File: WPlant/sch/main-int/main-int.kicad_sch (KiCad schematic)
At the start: 70 parts, among them J1 PROG/JTAG, J10 Ext, J8 eInk-Buttons, J9 Leak, M1 Motor_DC, Q6 Si2301, Q7 BC817, SW1 SW_Push, SW2 SW_Push, SW3 SW_Push, U1 SIWG917Y121MGABAR, U10 SP485EEN-L/TR, U11 TXU0102QDCURQ1, U5 TC4427AEOA713, U8 NC7S02P5, U9 INA180A2, X1 SIT1552AI-JE-DCC-32.768D

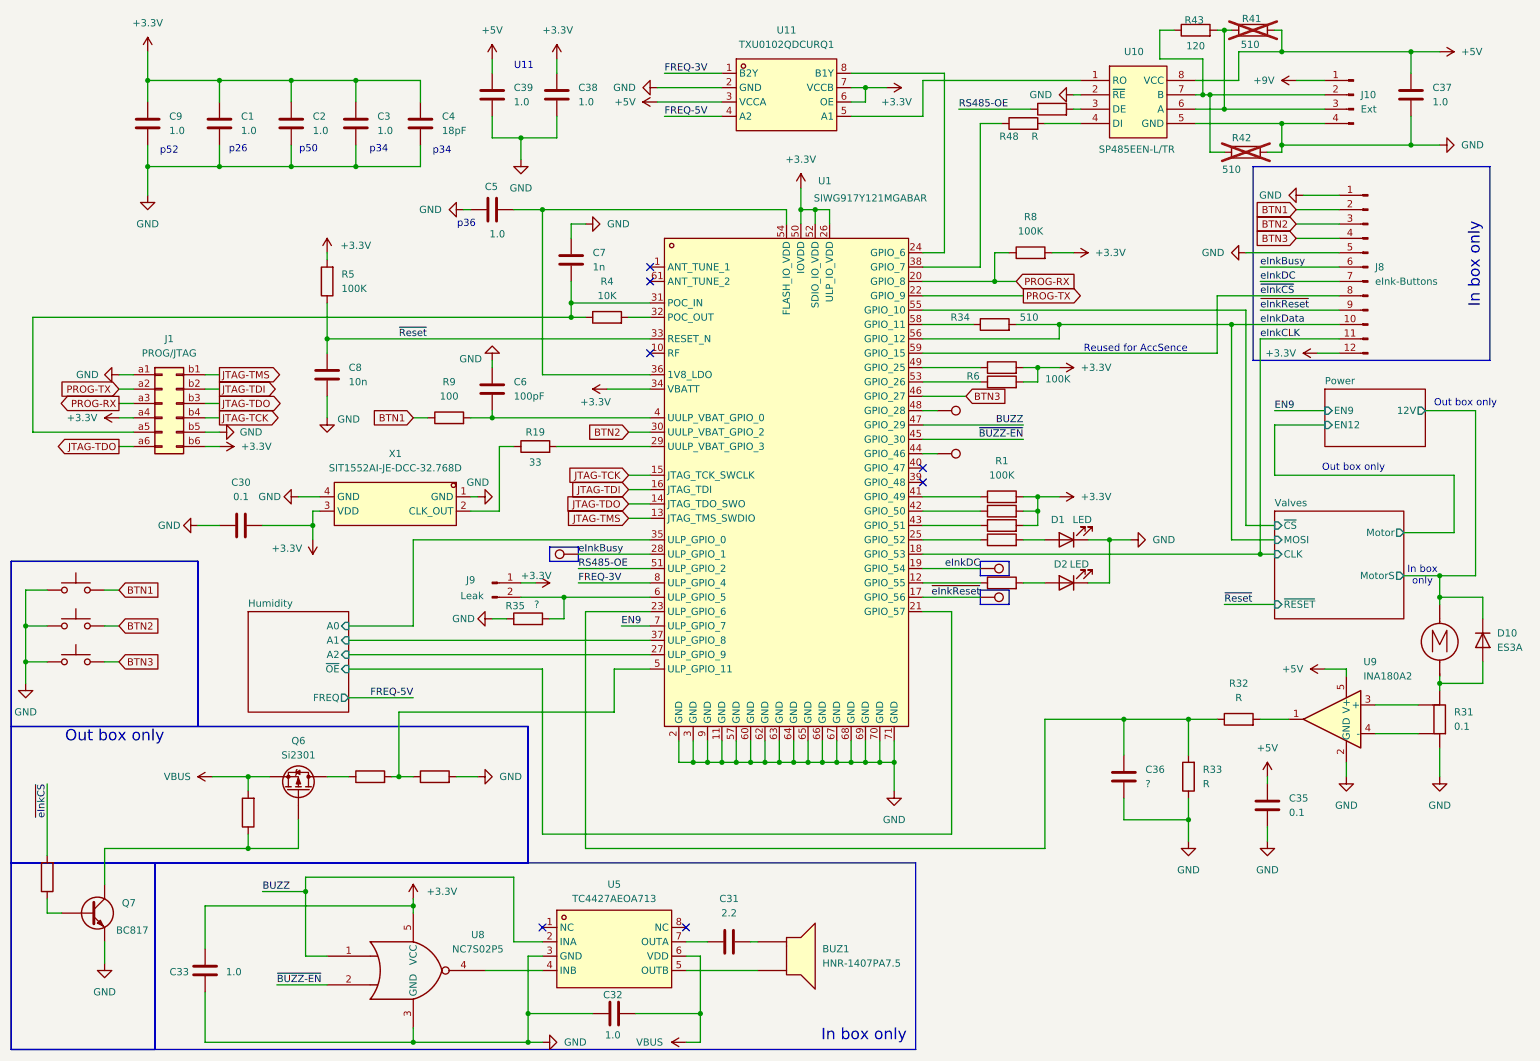
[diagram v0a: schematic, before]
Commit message: Generic design was splited to Main-Int and Main-Ext
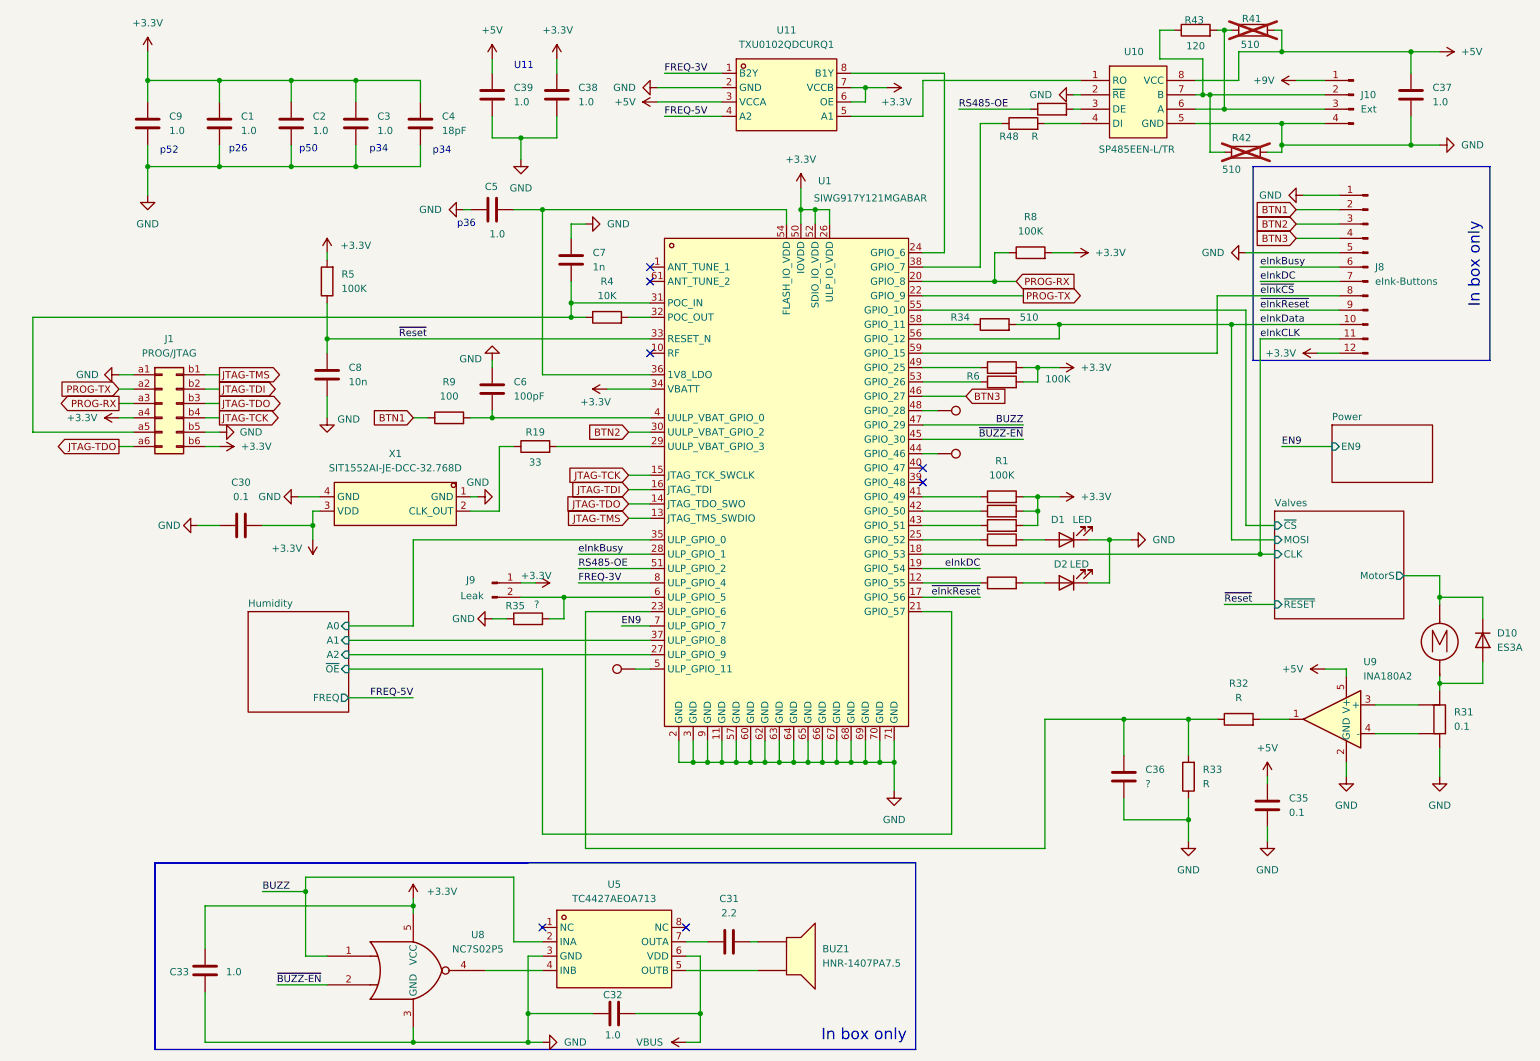
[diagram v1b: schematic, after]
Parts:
- removed Q6: Si2301, Package_TO_SOT_SMD:SOT-23, symbol Device:Q_PMOS_GSD
- removed Q7: BC817, Package_TO_SOT_SMD:SOT-23, symbol Transistor_BJT:BC817
- removed R36, R37, R38, R39: 100K, Resistor_SMD:R_0603_1608Metric_Pad0.98x0.95mm_HandSolder, symbol Device:R
- removed SW1, SW2, SW3: SW_Push, locals:KEY-TH_2P-L6.0-W3.5-P6.50, symbol Switch:SW_Push
- removed TP3, TP4, TP5: TestPoint, TestPoint:TestPoint_Pad_1.0x1.0mm, symbol Connector:TestPoint
- added TP6: TestPoint, TestPoint:TestPoint_Pad_1.0x1.0mm, symbol Connector:TestPoint
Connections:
- net at U1.5 (ULP_GPIO_11): now also TP6.1
- net Power/12V renamed Valves/MotorS
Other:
- sheet Power ports: added none; removed 12V, EN12
- sheet Valves ports: added none; removed Motor
- note removed: "In box only"
- note removed: "Out box only"
- note removed: "Reused for AccSence"

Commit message: Update SWIG917 footprint. Change footprint of LeakDetector
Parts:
- J9: footprint Connector_PinHeader_2.54mm:PinHeader_1x02_P2.54mm_Vertical -> Connector_JST:JST_XH_B2B-XH-A_1x02_P2.50mm_Vertical
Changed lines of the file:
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@@
 			)
 		)
-		(property "Footprint" "Connector_PinHeader_2.54mm:PinHeader_1x02_P2.54mm_Vertical"
+		(property "Footprint" "Connector_JST:JST_XH_B2B-XH-A_1x02_P2.50mm_Vertical"
 			(at 100.33 113.03 0)
 			(effects

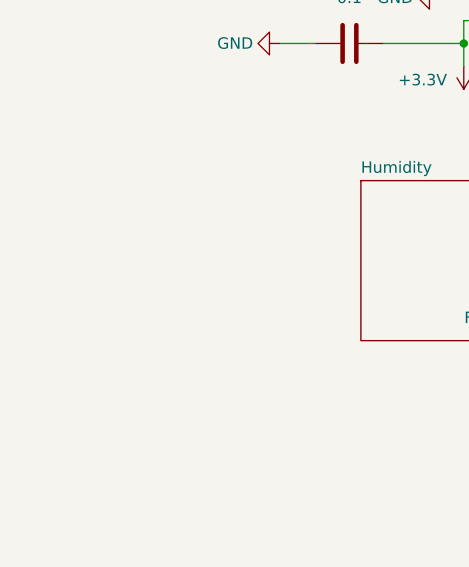
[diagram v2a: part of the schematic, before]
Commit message: Addeed places for latches on Extension board. Updated MainInt sch and pcb
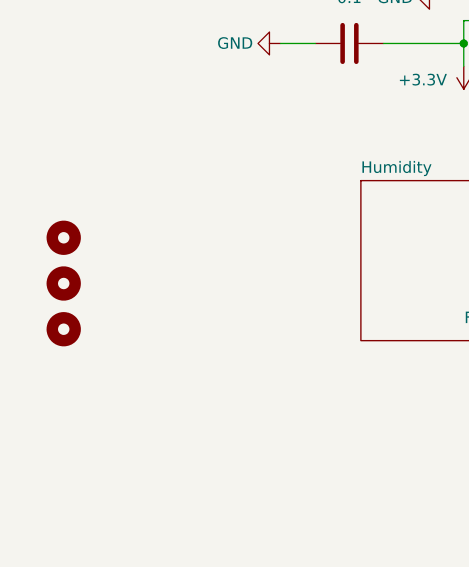
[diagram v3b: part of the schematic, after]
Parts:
- added H1, H2, H3: MountingHole, MountingHole:MountingHole_3.2mm_M3, symbol Mechanical:MountingHole
- C31: footprint Capacitor_SMD:C_0603_1608Metric_Pad1.08x0.95mm_HandSolder -> Capacitor_SMD:C_1206_3216Metric_Pad1.33x1.80mm_HandSolder
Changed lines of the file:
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@@
 	)
 	(symbol
+		(lib_id "Mechanical:MountingHole")
+		(at 24.13 129.54 0)
+		(unit 1)
+		(exclude_from_sim yes)
+		(in_bom no)
+		(on_board yes)
+		(dnp no)
+		(fields_autoplaced yes)
+		(property "Reference" "H2"
+			(at 26.67 128.2699 0)
+			(effects
+				(font
+					(size 1.27 1.27)
+				)
+				(justify left)
+				(hide yes)
+			)
+		)
+		(property "Value" "MountingHole"
+			(at 26.67 130.8099 0)
+			(effects
+				(font
+					(size 1.27 1.27)
+				)
+				(justify left)
+				(hide yes)
+			)
+		)
+		(property "Footprint" "MountingHole:MountingHole_3.2mm_M3"
+			(at 24.13 129.54 0)
+			(effects
+				(font
+					(size 1.27 1.27)
+				)
+				(hide yes)
+			)
+		)
+		(property "Datasheet" "~"
+			(at 24.13 129.54 0)
+			(effects
+				(font
+					(size 1.27 1.27)
+				)
+				(hide yes)
+			)
+		)
+		(property "Description" "Mounting Hole without connection"
+			(at 24.13 129.54 0)
+			(effects
+				(font
+					(size 1.27 1.27)
+				)
+				(hide yes)
+			)
+		)
+		(instances
+			(project "main-int"
+				(path "/71bd3f7f-463d-4a2c-bec7-ca56c2fe6cec"
+					(reference "H2")
+					(unit 1)
+				)
+			)
+		)
+	)
+	(symbol
 		(lib_id "power:+3.3V")
 		(at 107.95 113.03 270)
@@
 	)
 	(symbol
+		(lib_id "Mechanical:MountingHole")
+		(at 24.13 124.46 0)
+		(unit 1)
+		(exclude_from_sim yes)
+		(in_bom no)
+		(on_board yes)
+		(dnp no)
+		(fields_autoplaced yes)
+		(property "Reference" "H1"
+			(at 26.67 123.1899 0)
+			(effects
+				(font
+					(size 1.27 1.27)
+				)
+				(justify left)
+				(hide yes)
+			)
+		)
+		(property "Value" "MountingHole"
+			(at 26.67 125.7299 0)
+			(effects
+				(font
+					(size 1.27 1.27)
+				)
+				(justify left)
+				(hide yes)
+			)
+		)
+		(property "Footprint" "MountingHole:MountingHole_3.2mm_M3"
+			(at 24.13 124.46 0)
+			(effects
+				(font
+					(size 1.27 1.27)
+				)
+				(hide yes)
+			)
+		)
+		(property "Datasheet" "~"
+			(at 24.13 124.46 0)
+			(effects
+				(font
+					(size 1.27 1.27)
+				)
+				(hide yes)
+			)
+		)
+		(property "Description" "Mounting Hole without connection"
+			(at 24.13 124.46 0)
+			(effects
+				(font
+					(size 1.27 1.27)
+				)
+				(hide yes)
+			)
+		)
+		(instances
+			(project ""
+				(path "/71bd3f7f-463d-4a2c-bec7-ca56c2fe6cec"
+					(reference "H1")
+					(unit 1)
+				)
+			)
+		)
+	)
+	(symbol
 		(lib_id "power:+3.3V")
 		(at 68.58 105.41 180)
@@
 	)
 	(symbol
+		(lib_id "Mechanical:MountingHole")
+		(at 24.13 134.62 0)
+		(unit 1)
+		(exclude_from_sim yes)
+		(in_bom no)
+		(on_board yes)
+		(dnp no)
+		(fields_autoplaced yes)
+		(property "Reference" "H3"
+			(at 26.67 133.3499 0)
+			(effects
+				(font
+					(size 1.27 1.27)
+				)
+				(justify left)
+				(hide yes)
+			)
+		)
+		(property "Value" "MountingHole"
+			(at 26.67 135.8899 0)
+			(effects
+				(font
+					(size 1.27 1.27)
+				)
+				(justify left)
+				(hide yes)
+			)
+		)
+		(property "Footprint" "MountingHole:MountingHole_3.2mm_M3"
+			(at 24.13 134.62 0)
+			(effects
+				(font
+					(size 1.27 1.27)
+				)
+				(hide yes)
+			)
+		)
+		(property "Datasheet" "~"
+			(at 24.13 134.62 0)
+			(effects
+				(font
+					(size 1.27 1.27)
+				)
+				(hide yes)
+			)
+		)
+		(property "Description" "Mounting Hole without connection"
+			(at 24.13 134.62 0)
+			(effects
+				(font
+					(size 1.27 1.27)
+				)
+				(hide yes)
+			)
+		)
+		(instances
+			(project "main-int"
+				(path "/71bd3f7f-463d-4a2c-bec7-ca56c2fe6cec"
+					(reference "H3")
+					(unit 1)
+				)
+			)
+		)
+	)
+	(symbol
 		(lib_id "power:GND")
 		(at 100.33 119.38 270)
@@
 			)
 		)
-		(property "Footprint" "Capacitor_SMD:C_0603_1608Metric_Pad1.08x0.95mm_HandSolder"
+		(property "Footprint" "Capacitor_SMD:C_1206_3216Metric_Pad1.33x1.80mm_HandSolder"
 			(at 146.05 175.5648 0)
 			(effects

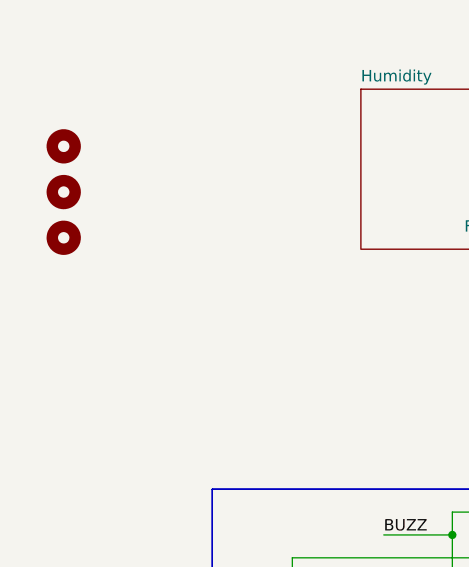
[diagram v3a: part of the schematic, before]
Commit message: Route of MainInt PCB almost done
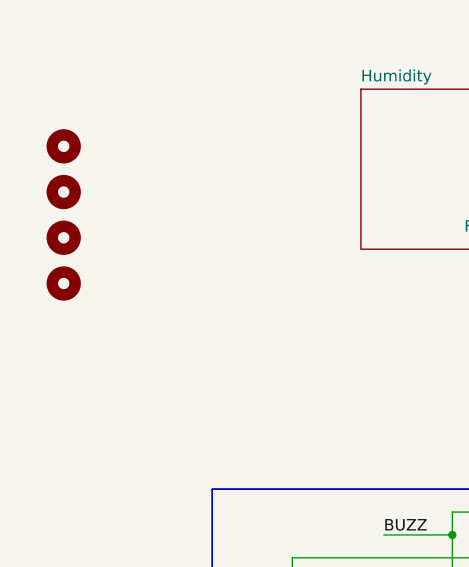
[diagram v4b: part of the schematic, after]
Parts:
- added H4: MountingHole, MountingHole:MountingHole_3.2mm_M3, symbol Mechanical:MountingHole
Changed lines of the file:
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@@
+	)
+	(symbol
+		(lib_id "Mechanical:MountingHole")
+		(at 24.13 139.7 0)
+		(unit 1)
+		(exclude_from_sim yes)
+		(in_bom no)
+		(on_board yes)
+		(dnp no)
+		(fields_autoplaced yes)
+		(property "Reference" "H4"
+			(at 26.67 138.4299 0)
+			(effects
+				(font
+					(size 1.27 1.27)
+				)
+				(justify left)
+				(hide yes)
+			)
+		)
+		(property "Value" "MountingHole"
+			(at 26.67 140.9699 0)
+			(effects
+				(font
+					(size 1.27 1.27)
+				)
+				(justify left)
+				(hide yes)
+			)
+		)
+		(property "Footprint" "MountingHole:MountingHole_3.2mm_M3"
+			(at 24.13 139.7 0)
+			(effects
+				(font
+					(size 1.27 1.27)
+				)
+				(hide yes)
+			)
+		)
+		(property "Datasheet" "~"
+			(at 24.13 139.7 0)
+			(effects
+				(font
+					(size 1.27 1.27)
+				)
+				(hide yes)
+			)
+		)
+		(property "Description" "Mounting Hole without connection"
+			(at 24.13 139.7 0)
+			(effects
+				(font
+					(size 1.27 1.27)
+				)
+				(hide yes)
+			)
+		)
+		(instances
+			(project "main-int"
+				(path "/71bd3f7f-463d-4a2c-bec7-ca56c2fe6cec"
+					(reference "H4")
+					(unit 1)
+				)
+			)
+		)
 	)
 	(symbol

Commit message: Route of MainInt PCB done
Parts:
- J8: footprint easyeda2kicad:CONN-TH_XAD-12A -> locals:CONN-TH_XAD-12AS
- U1: footprint easyeda2kicad:COMM-SMD_SIWG917Y110LGNBA -> locals:COMM-SMD_SIWG917Y110LGNBA
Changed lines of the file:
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@@
 			)
 		)
-		(property "Footprint" "easyeda2kicad:COMM-SMD_SIWG917Y110LGNBA"
+		(property "Footprint" "locals:COMM-SMD_SIWG917Y110LGNBA"
 			(at 152.4 148.59 0)
 			(effects
@@
 			)
 		)
-		(property "Footprint" "easyeda2kicad:CONN-TH_XAD-12A"
+		(property "Footprint" "locals:CONN-TH_XAD-12AS"
 			(at 255.27 57.15 0)
 			(effects
